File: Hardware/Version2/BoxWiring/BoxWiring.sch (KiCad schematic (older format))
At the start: 15 parts, among them K1 Internal/External, K2 6V/12V Select, K3 Heat/Cool Select, P1 Conn_WallPlug_Earth, SW1 SW_SPST, T1 0030130207-TFRM, T2 0030130208-TFRM, T3 F-213Z_XFRM, T4 VPS24-7300_XFRM, U1 TMP36GT9, U2 TMP36GT9, U3 Control_Board, U4 TM1638Module

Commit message: Added TM1638 Displays
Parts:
- added M? (x2): Fan, symbol Motor:Fan
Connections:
- net +12VDC: no longer K3.11
- net BAT+: now also K1.22; no longer K1.24
- net GND: now also M?.2 (-)
- net VBAT_INT: now also K1.24; no longer K1.22
- new net: M?.1 (+), M?.2 (-)
- new net OvenSupply: K3.11, M?.1 (+)
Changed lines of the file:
@@
 BAT-
-Wire Wire Line
-	5850 3000 5850 3500
 Wire Wire Line
 	6250 3000 6250 3200
@@
 Text Label 4450 4850 0    50   ~ 0
 VBAT_INT
-Text Label 6050 3000 3    50   ~ 0
+Text Label 5850 3000 3    50   ~ 0
 VBAT_INT
 Text Label 5950 2100 1    50   ~ 0
@@
 Text Label 7000 5850 2    50   ~ 0
 OVEN-
-Text Label 7000 5450 2    50   ~ 0
-+12VDC
 Wire Wire Line
 	7600 5350 7850 5350
@@
 Text Label 7000 5050 2    50   ~ 0
 Heat_Cool_Sel
+Text Label 7000 5450 2    50   ~ 0
+OvenSupply
+$Comp
+L Motor:Fan M?
+U 1 1 5FDA010B
+P 8800 5700
+F 0 "M?" H 8958 5796 50  0000 L CNN
+F 1 "Fan" H 8958 5705 50  0000 L CNN
+F 2 "" H 8800 5710 50  0001 C CNN
+F 3 "~" H 8800 5710 50  0001 C CNN
+	1    8800 5700
+	1    0    0    -1
+$EndComp
+$Comp
+L Motor:Fan M?
+U 1 1 5FDA1241
+P 8800 6250
+F 0 "M?" H 8958 6346 50  0000 L CNN
+F 1 "Fan" H 8958 6255 50  0000 L CNN
+F 2 "" H 8800 6260 50  0001 C CNN
+F 3 "~" H 8800 6260 50  0001 C CNN
+	1    8800 6250
+	1    0    0    -1
+$EndComp
+Wire Wire Line
+	8800 5900 8800 5950
+Wire Wire Line
+	8800 6450 6900 6450
+$Comp
+L power:GND #PWR?
+U 1 1 5FDACDCA
+P 6900 6450
+F 0 "#PWR?" H 6900 6200 50  0001 C CNN
+F 1 "GND" H 6905 6277 50  0000 C CNN
+F 2 "" H 6900 6450 50  0001 C CNN
+F 3 "" H 6900 6450 50  0001 C CNN
+	1    6900 6450
+	1    0    0    -1
+$EndComp
+Wire Wire Line
+	8800 4600 6975 4600
+Wire Wire Line
+	8800 4600 8800 5400
+Text Label 6975 4600 2    50   ~ 0
+OvenSupply
+Wire Wire Line
+	5850 3500 5850 3425
+Wire Wire Line
+	5850 3425 6050 3425
+Wire Wire Line
+	6050 3425 6050 3000
 $EndSCHEMATC

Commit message: added mechanical dwgs
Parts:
- removed M? (x2): Fan, symbol Motor:Fan
- removed T3: F-213Z_XFRM, symbol BoxWiring-rescue:F-213Z_XFRM-F100B200TestPanel
- removed T4: VPS24-7300_XFRM, symbol BoxWiring-rescue:VPS24-7300_XFRM-F100B200TestPanel
- removed U2: TMP36GT9, XDCR_TMP36GT9, symbol BoxWiring-rescue:TMP36GT9-F100B200TestPanel
- removed U3: Control_Board, symbol BoxWiring-rescue:Control_Board-F100B200TestPanel
- removed U4: TM1638Module, symbol BoxWiring-rescue:TM1638Module-F100B200TestPanel
- added BT1: External_bat, symbol Device:Battery
- added CB1: C-1893, symbol BoxWiring-rescue:C-1893
- added CBL1, CBL2: MICRO_A_TO_MICRO_A, symbol BoxWiring-rescue:MICRO_A_TO_MICRO_A
- added CBL3: CNT_CABLE_5, symbol BoxWiring-rescue:CNT_CABLE_5
- added CBL4, CBL5: CNT_CABLE_12, symbol BoxWiring-rescue:CNT_CABLE_12
- added CBL6: CNT_CABLE_4, symbol BoxWiring-rescue:CNT_CABLE_4
- added CBL7, CBL8: DSP_CBL, symbol BoxWiring-rescue:DSP_CBL
- added F1, F2: Fuse, symbol Device:Fuse
- added J1: Conn_01x12_Male, symbol Connector:Conn_01x12_Male
- added J2, J7: Conn_01x12_Female, symbol Connector:Conn_01x12_Female
- added J3: Conn_01x04_Male, symbol Connector:Conn_01x04_Male
- added J4: Conn_01x04_Female, symbol Connector:Conn_01x04_Female
- added J5: Conn_01x03_Female, symbol Connector:Conn_01x03_Female
- added J6: Conn_01x03_Male, symbol Connector:Conn_01x03_Male
- added J8, J9: USB_A_TO_B_PNLMNT, symbol BoxWiring-rescue:USB_A_TO_B_PNLMNT
- added K4: On/Off, Relay_THT:Relay_DPDT_Finder_40.52, symbol BoxWiring-rescue:12VDCRelay2906223-F100B200TestPanel
- added LA1: Lamp, symbol Device:Lamp
- added M1, M2, M3, M4: Fan, symbol Motor:Fan
- added P2: Conn_WallPlug, symbol Connector:Conn_WallPlug
- added R1, R2: Heater, symbol Device:Heater
- added SW2: SW_SPST, symbol Switch:SW_SPST
- added SW3: SW_Push, symbol Switch:SW_Push
- added U2, U4: UUT, symbol BoxWiring-rescue:UUT
- added U3: Control_Board-F100B200TestPanel, symbol BoxWiring-rescue:Control_Board-F100B200TestPanel-BoxWiring-rescue
- added U5: EL240A20R-12, symbol Relay_SolidState:S216S01
- added U6: AD1072_PS, symbol BoxWiring-rescue:AD1072_PS
- added U7: ERPF-400-12, symbol BoxWiring-rescue:ERPF-400-12
- added U8, U9: TM1637_DISPLAY, symbol BoxWiring-rescue:TM1637_DISPLAY
- K1, K2, K3: Description (none) -> RELAY GEN PURPOSE DPDT 8A 12V; DigikeyPart# (none) -> 277-12082-ND; Mng (none) -> Phoenix Contact; MngPart# (none) -> 2906223
- SW1: Description (none) -> SWITCH TOGGLE SPST 20A 125V; DigikeyPart# (none) -> 432-1243-ND; Mng (none) -> Carling Technologies; MngPart# (none) -> 2FAA01-73
- U1: Description (none) -> SENSOR TEMP 2.7/5.5 TO92-3; DigikeyPart# (none) -> TMP36GT9-ND; Mng (none) -> Analog Devices Inc.; MngPart# (none) -> TMP36GT9
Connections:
- net +12VDC: now also J4.2 (Pin_2); no longer K1.A1, K2.A1
- net 5VDC: now also U3.J2_4 (5V1)
- net COMP_TEMP: now also J1.11 (Pin_11), U3.J1_7 (A1)
- net GND: now also BT1.2 (-), J1.12 (Pin_12), J1.5 (Pin_5), J4.4 (Pin_4), J6.3 (Pin_3), SW3.1, U6.2 (-), U6.4 (-), U6.5 (GND), U7.4 (-V), U7.5 (-V), U7.6 (-V), U7.7 (GND), U8.GND, U9.GND; no longer K1.12, K1.14, T1.YEL (SC), T2.YEL (SC)
- net OVEN_TEMP: now also J6.2 (Pin_2), U3.J1_8 (A0); no longer U1.2 (VOUT)
- net at U1.3 (GND): now also J5.3 (Pin_3)
- net at U1.1 (+VS): now also J5.1 (Pin_1)
- net at PE1.1, PE2.1: now also J3.3 (Pin_3); no longer K3.12, K3.24
- net at PE1.2, PE2.2: now also J3.2 (Pin_2), M1.1 (+), M2.1 (+), M3.1 (+), M4.1 (+), U5.3; no longer K3.14, K3.22
- net AC_N: now reaches P1.2 (AC_N), T1.WHITE (AB), T2.WHITE (AB)
- net AC_N: now also U6.6 (N), U7.8 (N)
- net AC_SW: now reaches T1.BLACK (AA), T2.BLACK (AA)
- net AC_SW: now also F2.2, U6.7 (L), U7.9 (L); no longer SW1.1 (A)
- net 6V-12V_SEL renamed 6V_12V_SEL
- net 6V_12V_SEL: now also U3.J5_5 (DOUT_3)
- net BAT+: no longer names the net of K1.22
- net EXT-INT_SEL renamed INTER_EXTER_SEL
- net INTER_EXTER_SEL: now also U3.J14_10 (DOUT_8)
- net OVEN- renamed OVEN_DRIVE
- net OVEN_DRIVE: now also U3.J6_2 (OVEN_DRV)
- net OvenSupply: no longer names the net of K3.11
- net UUT_AC1: no longer names the net of K2.11
- net UUT_AC1: now also K4.14
- net UUT_AC2: no longer names the net of K2.21
- net UUT_AC2: now also K4.24
- net UUT_B+: no longer names the net of K1.21
- net UUT_B- renamed VIN_MINUS
- net VIN_MINUS: now also U3.~ (Vin_Plus)
- net VBAT_INT: no longer names the net of K1.24
- new net: J5.2 (Pin_2), U1.2 (VOUT)
- new net: BT1.1 (+), K1.12
- new net: J4.1 (Pin_1), K3.22
- new net: J4.3 (Pin_3), K3.24
- new net: J1.3 (Pin_3), T1.YEL (SC), T2.YEL (SC)
- new net: F2.1, SW1.1 (A)
- new net: R2.2, U5.1
- new net: R1.2, U5.2
- new net: J3.1 (Pin_1), U5.4
- new net: J3.4 (Pin_4), M1.2 (-), M2.2 (-), M3.2 (-), M4.2 (-)
- new net: F1.2, LA1.2 (+), R1.1
- new net: LA1.1 (-), P2.2 (AC_N), R2.1
- new net: P2.1 (AC_P), SW2.1 (A)
- new net: F1.1, SW2.2 (B)
- new net: U3.J2_2 (GND3), U3.J2_3 (GND2)
- new net: SW3.2, U3.J2_6 (RST1)
- new net: J2.1 (Pin_1), U4.1 (AC_1)
- new net: J2.10 (Pin_10), U4.10 (3.3VDC)
- new net: J2.11 (Pin_11), U4.11 (COMP_TEMP)
- new net: J2.12 (Pin_12), U4.12 (GND)
- new net: J2.2 (Pin_2), U4.2 (AC_2)
- new net: J2.3 (Pin_3), U4.3 (AC_CT)
- new net: J2.4 (Pin_4), U4.4 (BAT+)
- new net: J2.5 (Pin_5), U4.5 (BAT-)
- new net: J2.6 (Pin_6), U4.6 (STAT_1)
- new net: J2.7 (Pin_7), U4.7 (STAT_2)
- new net: J2.8 (Pin_8), U4.8 (POWER_ON_NOT)
- new net: J2.9 (Pin_9), U4.9 (PLUS_LOAD)
- new net: J1.1 (Pin_1), K4.11
- new net: J1.2 (Pin_2), K4.21
- new net: J7.1 (Pin_1), U2.1 (AC_1)
- new net: J7.10 (Pin_10), U2.10 (3.3VDC)
- new net: J7.11 (Pin_11), U2.11 (COMP_TEMP)
- new net: J7.12 (Pin_12), U2.12 (GND)
- new net: J7.2 (Pin_2), U2.2 (AC_2)
- new net: J7.3 (Pin_3), U2.3 (AC_CT)
- new net: J7.4 (Pin_4), U2.4 (BAT+)
- new net: J7.5 (Pin_5), U2.5 (BAT-)
- new net: J7.6 (Pin_6), U2.6 (STAT_1)
- new net: J7.7 (Pin_7), U2.7 (STAT_2)
- new net: J7.8 (Pin_8), U2.8 (POWER_ON_NOT)
- new net: J7.9 (Pin_9), U2.9 (PLUS_LOAD)
- new net +24VDC: U6.1 (+), U6.3 (+)
- new net 12VDC: K1.A1, K2.A1, K4.A1, U3.J2_1 (VIN), U3.J6_1 (12VDC), U3.J7_4 (12VDC), U7.1 (+V), U7.2 (+V), U7.3 (+V)
- new net 3_3VDC: J1.10 (Pin_10), J6.1 (Pin_1), U3.J2_5 (3V3), U8.Vcc, U9.Vcc
- new net BAT_SIM: K1.14, U3.J7_1 (BAT_SIM)
- new net DSP1_CLK: U3.J16_17 (D22), U8.CLK
- new net DSP1_DIO: U3.J18_17 (D23), U8.DIO
- new net DSP2_CLK: U3.J16_16 (D24), U9.CLK
- new net DSP2_DIO: U3.J18_16 (D25), U9.DIO
- new net HEAT_COOL_SEL: U3.J5_6 (DOUT_2)
- new net ON_OFF: K4.A2, U3.J14_9 (DOUT_9)
- new net PLUS_LOAD: J1.9 (Pin_9), U3.J5_4 (DIN_4)
- new net POW_ON_NOT: J1.8 (Pin_8), U3.J5_3 (DIN_5)
- new net STAT_1: J1.6 (Pin_6), U3.J5_1 (DIN_7)
- new net STAT_2: J1.7 (Pin_7), U3.J5_2 (DIN_6)
- new net VIN_PLUS: J1.4 (Pin_4), U3.~ (Vin_Plus)
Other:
- note added: "CABINET"
- note added: "DSP1"
- note added: "DSP2"
- note added: "NATIVE_USB"
- note added: "OVEN"
- note added: "OVEN_POWER_CNT"
- note added: "OVEN_TEMP_SENSE"
- note added: "OVEN_UUT_CBL"
- note added: "PROGRAM_PORT"
- note added: "UUT_CABLE"
- note removed: "BAT"
- note removed: "UUT"
- moved on the sheet: K1, K2, K3, P1, SW1, T1, T2, U1

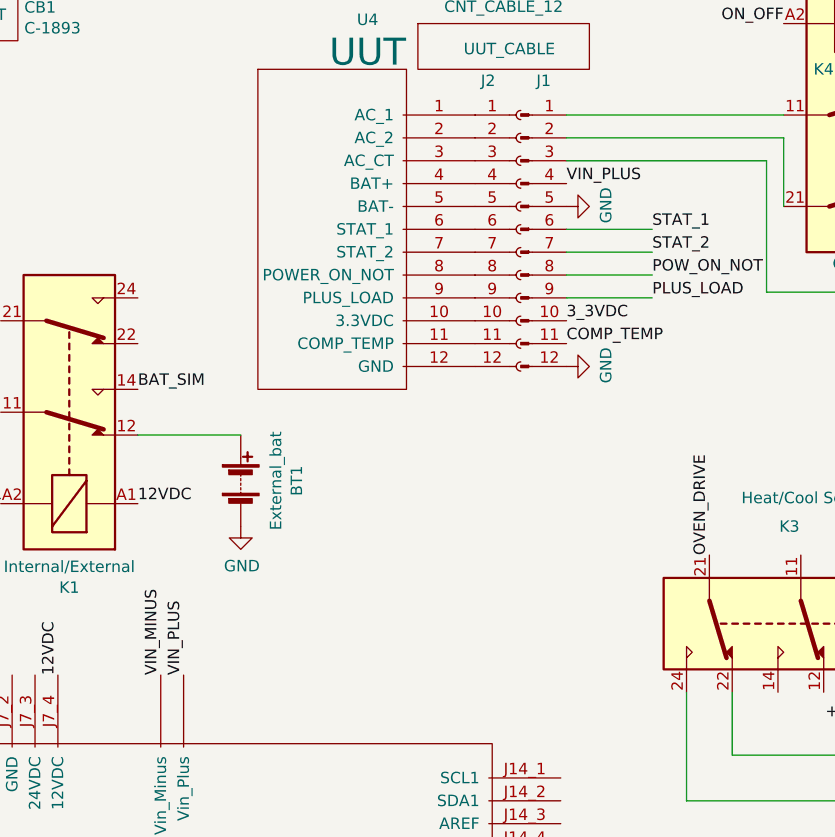
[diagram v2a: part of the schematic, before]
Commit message: changed to tkinter build with page changed to python venv
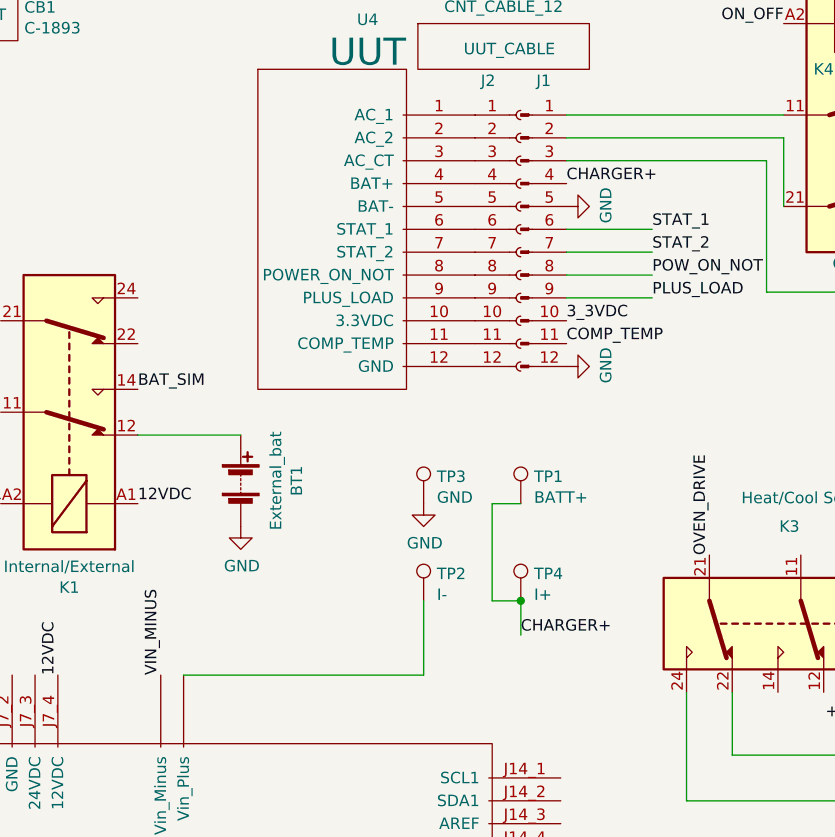
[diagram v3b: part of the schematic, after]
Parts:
- added TP1: BATT+, symbol Connector:TestPoint
- added TP2: I-, symbol Connector:TestPoint
- added TP3: GND, symbol Connector:TestPoint
- added TP4: I+, symbol Connector:TestPoint
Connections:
- net GND: now also TP3.1
- net VIN_PLUS renamed CHARGER+
- net CHARGER+: now also TP1.1, TP4.1; no longer U3.~ (Vin_Plus)
- new net: TP2.1, U3.~ (Vin_Plus)
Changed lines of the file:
@@
 Text Label 7950 750  2    50   ~ 0
 6V_12V_SEL
-Text Label 5750 1375 0    50   ~ 0
-VIN_PLUS
 $Comp
 L power:GND #PWR05
@@
 Text Label 3975 3525 1    50   ~ 0
 VIN_MINUS
-Text Label 4075 3525 1    50   ~ 0
-VIN_PLUS
 Text Label 5725 5475 0    50   ~ 0
 6V_12V_SEL
@@
 $EndComp
 Connection ~ 1275 4525
+$Comp
+L Connector:TestPoint TP3
+U 1 1 603509E7
+P 5125 2775
+F 0 "TP3" H 5183 2893 50  0000 L CNN
+F 1 "GND" H 5183 2802 50  0000 L CNN
+F 2 "" H 5325 2775 50  0001 C CNN
+F 3 "~" H 5325 2775 50  0001 C CNN
+	1    5125 2775
+	1    0    0    -1
+$EndComp
+$Comp
+L Connector:TestPoint TP1
+U 1 1 60352753
+P 5550 2775
+F 0 "TP1" H 5608 2893 50  0000 L CNN
+F 1 "BATT+" H 5608 2802 50  0000 L CNN
+F 2 "" H 5750 2775 50  0001 C CNN
+F 3 "~" H 5750 2775 50  0001 C CNN
+	1    5550 2775
+	1    0    0    -1
+$EndComp
+$Comp
+L Connector:TestPoint TP4
+U 1 1 60353A86
+P 5550 3200
+F 0 "TP4" H 5608 3318 50  0000 L CNN
+F 1 "I+" H 5608 3227 50  0000 L CNN
+F 2 "" H 5750 3200 50  0001 C CNN
+F 3 "~" H 5750 3200 50  0001 C CNN
+	1    5550 3200
+	1    0    0    -1
+$EndComp
+$Comp
+L Connector:TestPoint TP2
+U 1 1 603541A8
+P 5125 3200
+F 0 "TP2" H 5183 3318 50  0000 L CNN
+F 1 "I-" H 5183 3227 50  0000 L CNN
+F 2 "" H 5325 3200 50  0001 C CNN
+F 3 "~" H 5325 3200 50  0001 C CNN
+	1    5125 3200
+	1    0    0    -1
+$EndComp
+Wire Wire Line
+	5125 3525 5125 3200
+Wire Wire Line
+	4075 3525 5125 3525
+Text Label 5750 1375 0    50   ~ 0
+CHARGER+
+Wire Wire Line
+	5550 3350 5550 3200
+$Comp
+L power:GND #PWR?
+U 1 1 6036A238
+P 5125 2775
+F 0 "#PWR?" H 5125 2525 50  0001 C CNN
+F 1 "GND" H 5130 2602 50  0000 C CNN
+F 2 "" H 5125 2775 50  0001 C CNN
+F 3 "" H 5125 2775 50  0001 C CNN
+	1    5125 2775
+	1    0    0    -1
+$EndComp
+Wire Wire Line
+	5550 2775 5425 2775
+Wire Wire Line
+	5425 2775 5425 3200
+Wire Wire Line
+	5425 3200 5550 3200
+Connection ~ 5550 3200
+Text Label 5550 3350 0    50   ~ 0
+CHARGER+
 $EndSCHEMATC
